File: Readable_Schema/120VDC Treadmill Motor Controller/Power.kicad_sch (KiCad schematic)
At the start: 23 parts, among them J1 TB005-762-03BE, J6 TB0011-350-03BE, J7 OSTT7020150, K1 T9GV1L14-24, Q5 IPP60R060P7XKSA1, U5 TPSI3050QDWZRQ1

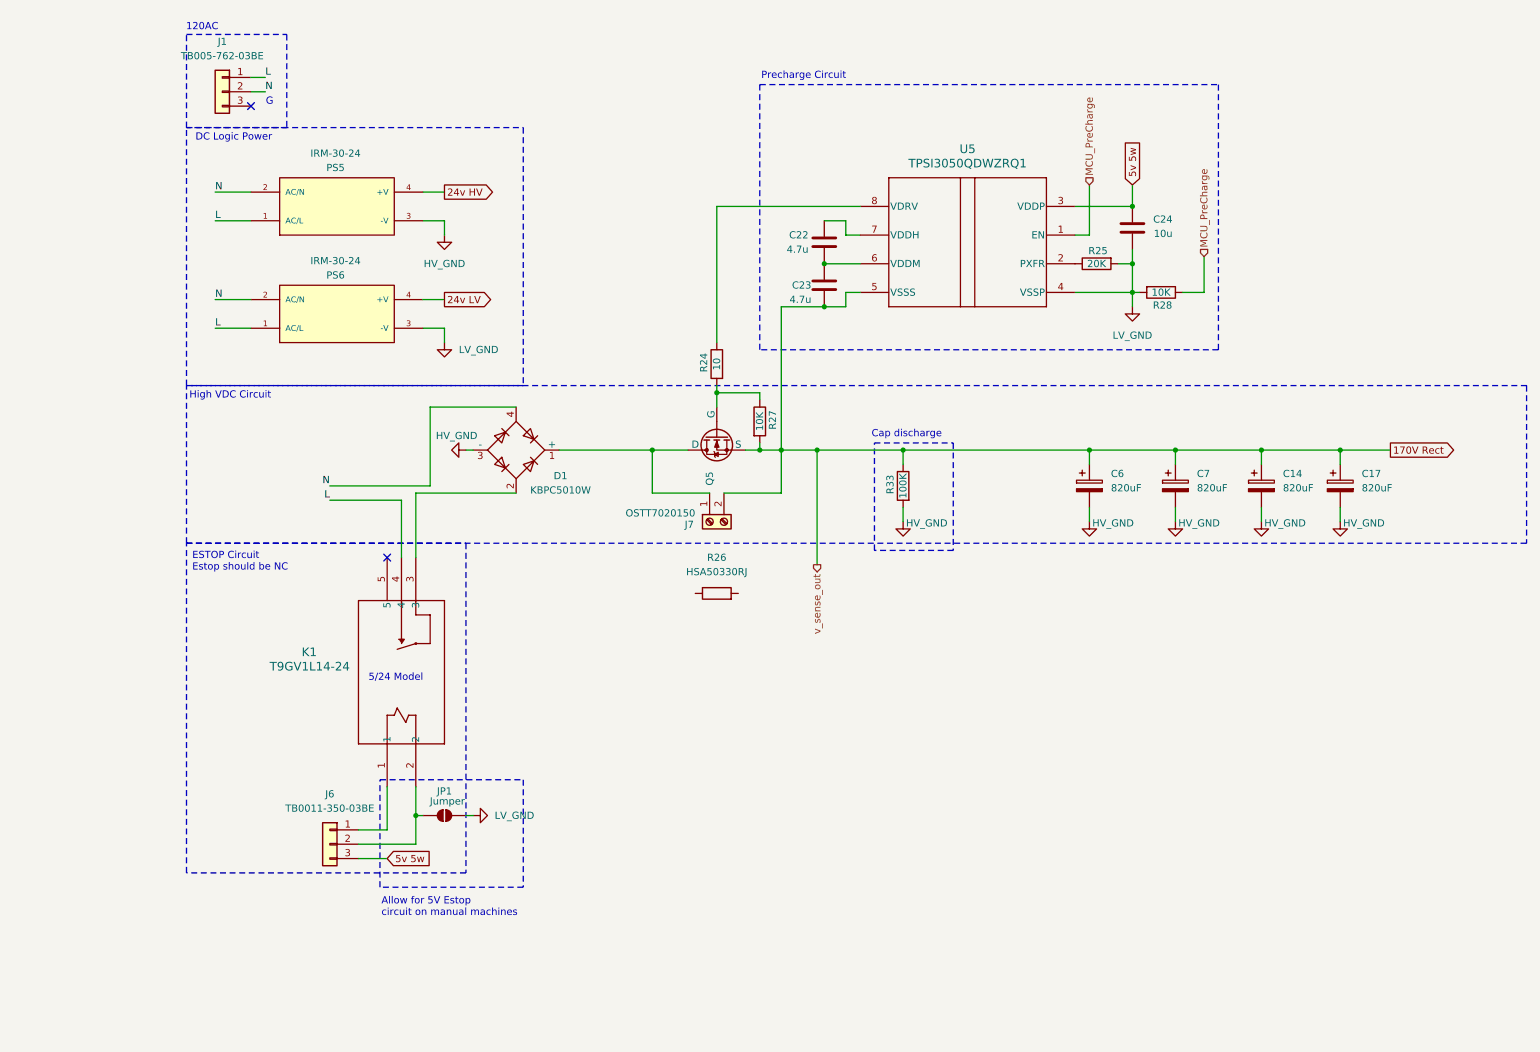
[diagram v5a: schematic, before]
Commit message: -Changed to a 15w 5v power supply instead of a 5w. (Achieved nothing else wtf)
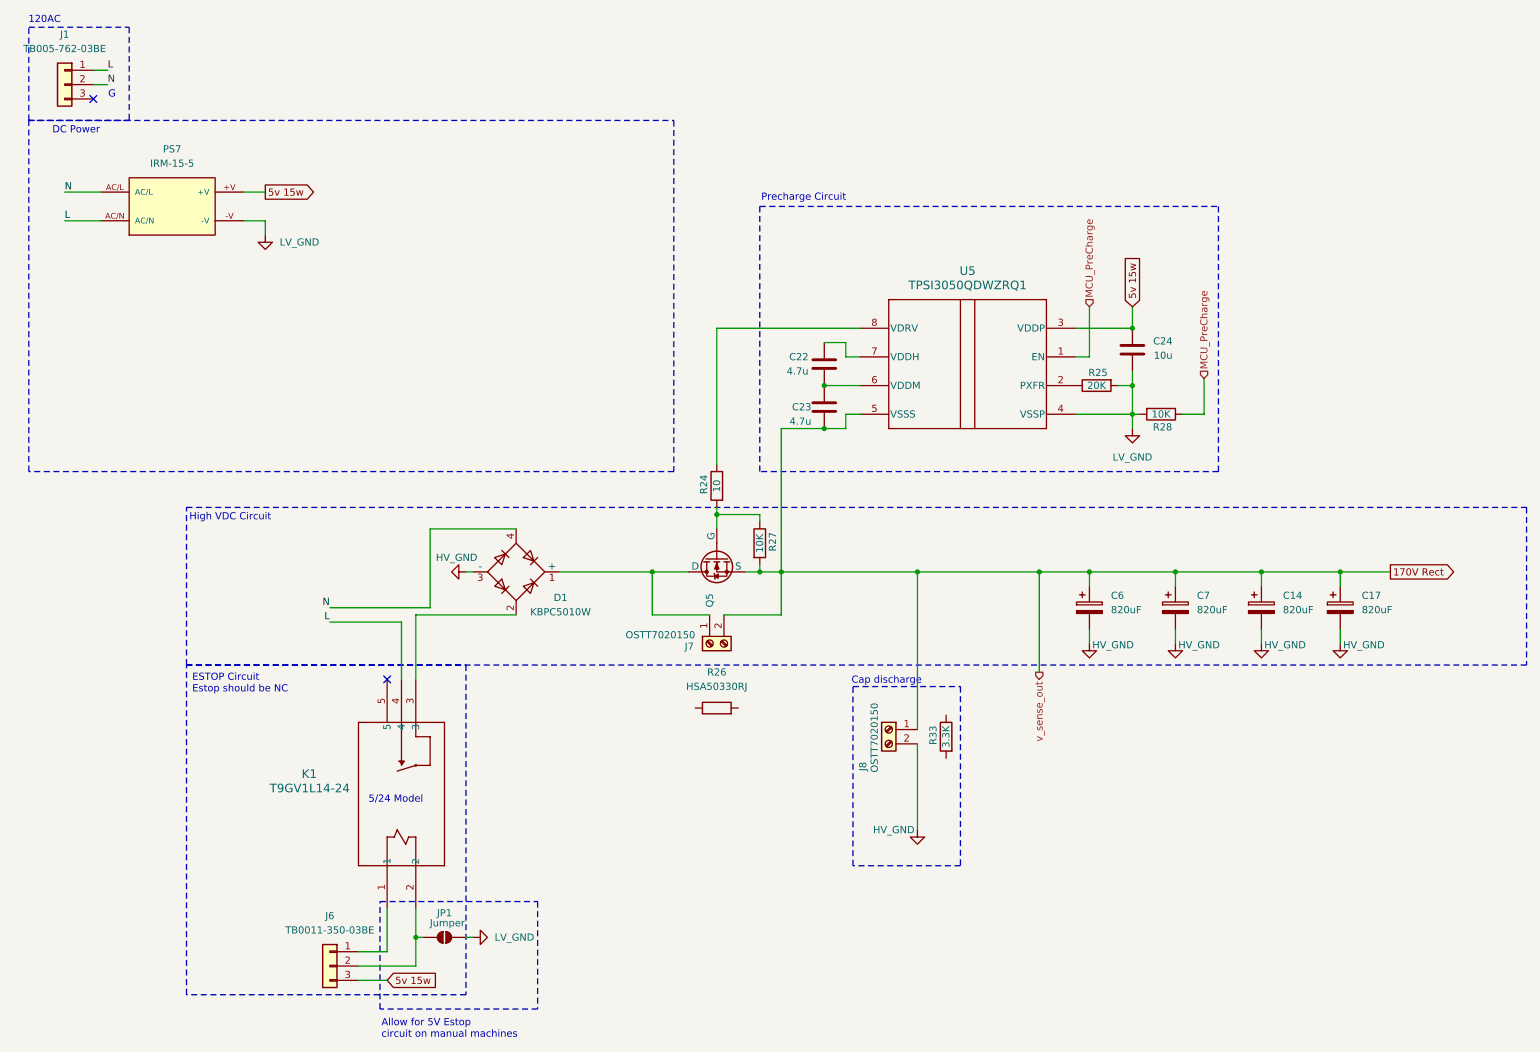
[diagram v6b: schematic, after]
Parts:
- removed PS5, PS6: IRM-30-24, Treadmill_Feet:CONV_IRM-30-24, symbol Treadmill_Comp:IRM-30-24
- added J8: OSTT7020150, Treadmill_Feet:CONN2_OSTT7020150_OST, symbol Connector:Screw_Terminal_01x02
- added PS7: IRM-15-5, Treadmill_Feet:CONV_IRM-15-5, symbol Treadmill_Comp:IRM-15-5
- R33: footprint Resistor_SMD:R_2512_6332Metric_Pad1.40x3.35mm_HandSolder -> (none)
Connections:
- net 170V Rect: now also J8.1 (Pin_1); no longer R33.1
- net HV_GND: now also J8.2 (Pin_2); no longer R33.2
- net L: now also PS7.AC/N
- net LV_GND: now also PS7.-V
- net N: now also PS7.AC/L
- net 5v 5w renamed 5v 15w
- net 5v 15w: now also PS7.+V
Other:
- note added: "DC Power"
- note removed: "DC Logic Power"
- moved on the sheet: C14, C17, C22, C23, C24, C6, C7, D1, J1, J6, J7, JP1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

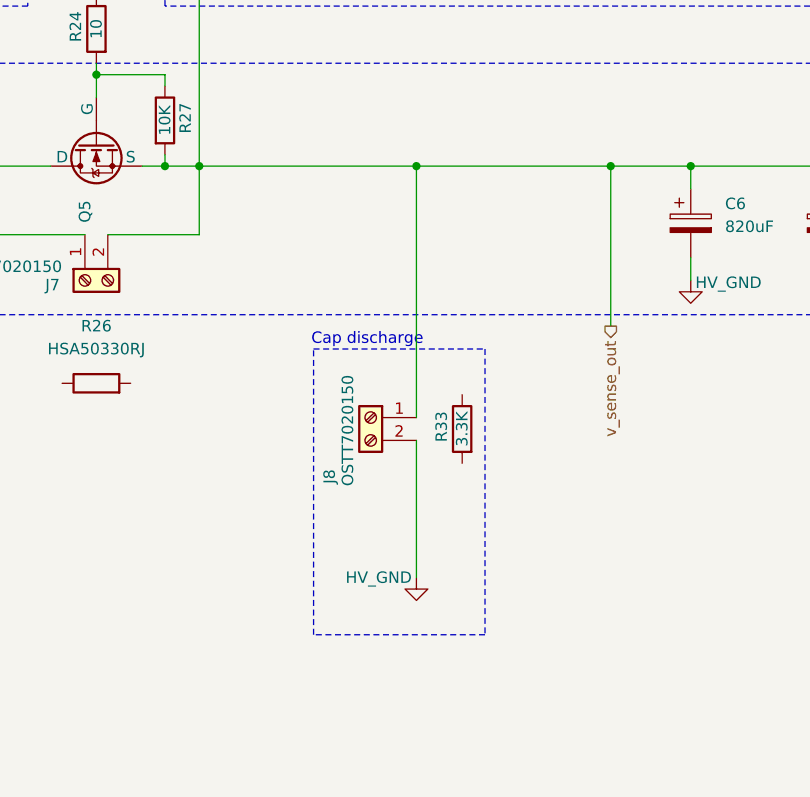
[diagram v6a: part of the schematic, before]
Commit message: -Added a more comprehensive discharge circuit --branch 1 uses a DNMOS with neg iso supply to do nothing when circuit is plugged in and to pull caps through 3.3K when circuit is off --Branch 2 passively pulls current from caps through 30K whilst powering a red LED to provide a visual that the circuit is dangerous
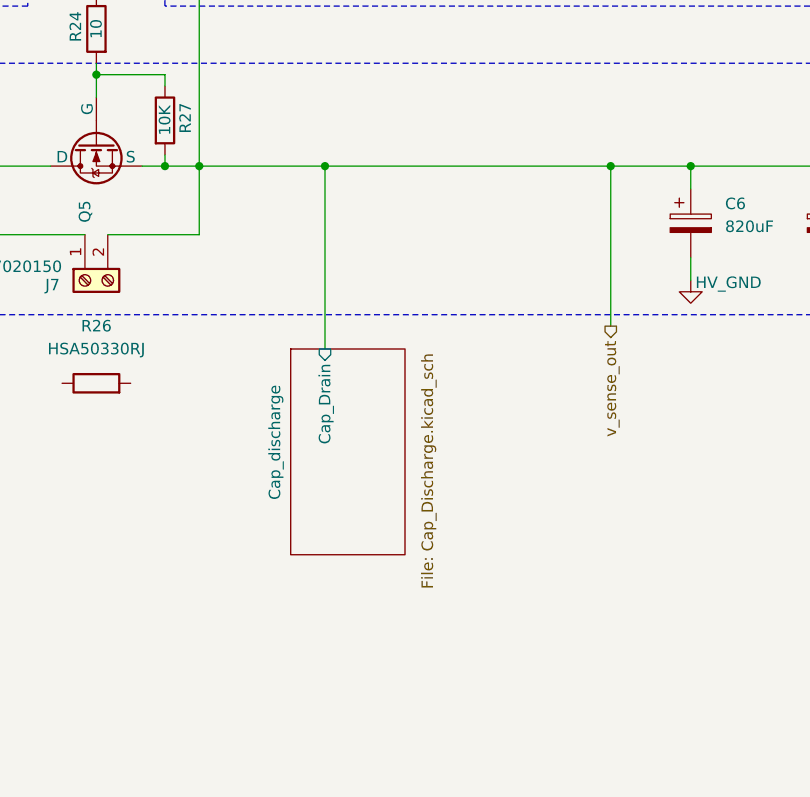
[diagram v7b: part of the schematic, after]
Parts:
- removed J8: OSTT7020150, Treadmill_Feet:CONN2_OSTT7020150_OST, symbol Connector:Screw_Terminal_01x02
- removed R33: HVCB2512FKC100K, symbol Device:R
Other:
- added sheet Cap_discharge (Cap_Discharge.kicad_sch)
- note removed: "Cap discharge"
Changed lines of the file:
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@@
 	)
 	(rectangle
-		(start 160.02 132.08)
-		(end 179.07 163.83)
-		(stroke
-			(width 0)
-			(type dot)
-			(color 255 255 0 1)
-		)
-		(fill
-			(type none)
-		)
-	)
-	(rectangle
 		(start 76.2 170.18)
 		(end 104.14 189.23)
@@
 		)
 	)
-	(text "Cap discharge"
-		(exclude_from_sim no)
-		(at 159.766 131.064 0)
-		(effects
-			(font
-				(size 1.27 1.27)
-				(color 255 255 0 1)
-			)
-			(justify left)
-		)
-	)
 	(text "120AC"
 		(exclude_from_sim no)
@@
 	)
 	(junction
-		(at 171.45 111.76)
+		(at 217.17 111.76)
 		(diameter 0)
 		(color 0 0 0 0)
 	)
 	(junction
-		(at 217.17 111.76)
+		(at 154.94 78.74)
 		(diameter 0)
 		(color 0 0 0 0)
 	)
 	(junction
-		(at 154.94 78.74)
+		(at 143.51 111.76)
 		(diameter 0)
 		(color 0 0 0 0)
 	)
 	(junction
-		(at 143.51 111.76)
+		(at 161.29 111.76)
 		(diameter 0)
 		(color 0 0 0 0)
@@
 	(wire
 		(pts
-			(xy 147.32 111.76) (xy 171.45 111.76)
+			(xy 147.32 111.76) (xy 161.29 111.76)
 		)
 		(stroke
@@
 	(wire
 		(pts
-			(xy 171.45 111.76) (xy 193.04 111.76)
-		)
-		(stroke
-			(width 0)
-			(type default)
-		)
-	)
-	(wire
-		(pts
 			(xy 135.89 101.6) (xy 135.89 104.14)
 		)
@@
 	(wire
 		(pts
-			(xy 171.45 111.76) (xy 171.45 139.7)
+			(xy 161.29 111.76) (xy 193.04 111.76)
 		)
 		(stroke
@@
 	(wire
 		(pts
+			(xy 161.29 111.76) (xy 161.29 132.08)
+		)
+		(stroke
+			(width 0)
+			(type default)
+		)
+	)
+	(wire
+		(pts
 			(xy 124.46 119.38) (xy 134.62 119.38)
 		)
@@
 	(wire
 		(pts
-			(xy 171.45 142.24) (xy 171.45 157.48)
-		)
-		(stroke
-			(width 0)
-			(type default)
-		)
-	)
-	(wire
-		(pts
 			(xy 20.32 49.53) (xy 26.67 49.53)
 		)
@@
 	)
 	(symbol
-		(lib_id "power:GND1")
-		(at 171.45 157.48 0)
-		(unit 1)
-		(exclude_from_sim no)
-		(in_bom yes)
-		(on_board yes)
-		(dnp no)
-		(property "Reference" "#PWR028"
-			(at 171.45 163.83 0)
-			(effects
-				(font
-					(size 1.27 1.27)
-				)
-				(hide yes)
-			)
-		)
-		(property "Value" "HV_GND"
-			(at 170.942 157.48 0)
-			(effects
-				(font
-					(size 1.27 1.27)
-				)
-				(justify right)
-			)
-		)
-		(property "Footprint" ""
-			(at 171.45 157.48 0)
-			(effects
-				(font
-					(size 1.27 1.27)
-				)
-				(hide yes)
-			)
-		)
-		(property "Datasheet" ""
-			(at 171.45 157.48 0)
-			(effects
-				(font
-					(size 1.27 1.27)
-				)
-				(hide yes)
-			)
-		)
-		(property "Description" "Power symbol creates a global label with name \"GND1\" , ground"
-			(at 171.45 157.48 0)
-			(effects
-				(font
-					(size 1.27 1.27)
-				)
-				(hide yes)
-			)
-		)
-		(pin "1"
-		)
-		(instances
-			(project "120VDC Treadmill Motor Controller"
-				(path "/319bc5c0-2dd5-4df3-a34b-9170833ebccd/1fa0373b-ff98-4bf0-acad-d32450f2dcd0"
-					(reference "#PWR028")
-					(unit 1)
-				)
-			)
-		)
-	)
-	(symbol
 		(lib_id "Treadmill_Comp:IRM-15-5")
 		(at 39.37 46.99 0)
@@
 	)
 	(symbol
-		(lib_id "Connector:Screw_Terminal_01x02")
-		(at 166.37 139.7 0)
-		(mirror y)
-		(unit 1)
-		(exclude_from_sim no)
-		(in_bom yes)
-		(on_board yes)
-		(dnp no)
-		(property "Reference" "J8"
-			(at 161.798 147.066 90)
-			(effects
-				(font
-					(size 1.27 1.27)
-				)
-				(justify left)
-			)
-		)
-		(property "Value" "OSTT7020150"
-			(at 163.83 147.32 90)
-			(effects
-				(font
-					(size 1.27 1.27)
-				)
-				(justify left)
-			)
-		)
-		(property "Footprint" "Treadmill_Feet:CONN2_OSTT7020150_OST"
-			(at 166.37 139.7 0)
-			(effects
-				(font
-					(size 1.27 1.27)
-				)
-				(hide yes)
-			)
-		)
-		(property "Datasheet" "https://mm.digikey.com/Volume0/opasdata/d220001/medias/docus/388/OSTT7xx0150.pdf"
-			(at 166.37 139.7 0)
-			(effects
-				(font
-					(size 1.27 1.27)
-				)
-				(hide yes)
-			)
-		)
-		(property "Description" "Generic screw terminal, single row, 01x02, script generated (kicad-library-utils/schlib/autogen/connector/)"
-			(at 166.37 139.7 0)
-			(effects
-				(font
-					(size 1.27 1.27)
-				)
-				(hide yes)
-			)
-		)
-		(pin "1"
-		)
-		(pin "2"
-		)
-		(instances
-			(project "120VDC Treadmill Motor Controller"
-				(path "/319bc5c0-2dd5-4df3-a34b-9170833ebccd/1fa0373b-ff98-4bf0-acad-d32450f2dcd0"
-					(reference "J8")
-					(unit 1)
-				)
-			)
-		)
-	)
-	(symbol
-		(lib_id "Device:R")
-		(at 176.53 140.97 0)
-		(mirror y)
-		(unit 1)
-		(exclude_from_sim no)
-		(in_bom yes)
-		(on_board no)
-		(dnp no)
-		(property "Reference" "R33"
-			(at 174.244 140.716 90)
-			(effects
-				(font
-					(size 1.27 1.27)
-				)
-			)
-		)
-		(property "Value" "HVCB2512FKC100K"
-			(at 176.53 140.97 90)
-			(effects
-				(font
-					(size 1.27 1.27)
-				)
-				(hide yes)
-			)
-		)
-		(property "Footprint" ""
-			(at 178.308 140.97 90)
-			(effects
-				(font
-					(size 1.27 1.27)
-				)
-				(hide yes)
-			)
-		)
-		(property "Datasheet" "https://www.digikey.com/en/products/detail/yageo/SQP20AJB-3K3/9167228"
-			(at 176.53 140.97 0)
-			(effects
-				(font
-					(size 1.27 1.27)
-				)
-				(hide yes)
-			)
-		)
-		(property "Description" "3.3K"
-			(at 176.53 140.97 90)
-			(effects
-				(font
-					(size 1.27 1.27)
-				)
-			)
-		)
-		(pin "1"
-		)
-		(pin "2"
-		)
-		(instances
-			(project "120VDC Treadmill Motor Controller"
-				(path "/319bc5c0-2dd5-4df3-a34b-9170833ebccd/1fa0373b-ff98-4bf0-acad-d32450f2dcd0"
-					(reference "R33")
-					(unit 1)
-				)
-			)
-		)
-	)
-	(symbol
 		(lib_id "Device:C_Polarized")
 		(at 246.38 118.11 0)
@@
 				)
 			)
+		)
+	)
+	(sheet
+		(at 157.48 132.08)
+		(size 12.7 22.86)
+		(exclude_from_sim no)
+		(in_bom yes)
+		(on_board yes)
+		(dnp no)
+		(stroke
+			(width 0.1524)
+			(type solid)
+		)
+		(fill
+			(color 0 0 0 0.0000)
+		)
+		(property "Sheetname" "Cap_discharge"
+			(at 156.464 148.844 90)
+			(effects
+				(font
+					(size 1.27 1.27)
+				)
+				(justify left bottom)
+			)
+		)
+		(property "Sheetfile" "Cap_Discharge.kicad_sch"
+			(at 171.958 158.75 90)
+			(effects
+				(font
+					(size 1.27 1.27)
+				)
+				(justify left top)
+			)
+		)
+		(pin "Cap_Drain" input
+			(at 161.29 132.08 90)
+			(effects
+				(font
+					(size 1.27 1.27)
+				)
+				(justify right)
+			)
+		)
+		(instances
+			(project "120VDC Treadmill Motor Controller"
+				(path "/319bc5c0-2dd5-4df3-a34b-9170833ebccd/1fa0373b-ff98-4bf0-acad-d32450f2dcd0"
+					(page "6")
+				)
+			)
